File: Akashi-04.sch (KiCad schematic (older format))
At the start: 14 parts, among them CN10 PPPC192LFBN-RC, CN7 PPPC192LFBN-RC

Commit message: Designe done
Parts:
- removed D3, D4: LED, LED_THT:LED_D3.0mm_Clear, symbol Device:LED
- removed R4: 1k, Resistor_THT:R_Axial_DIN0207_L6.3mm_D2.5mm_P10.16mm_Horizontal, symbol Device:R
- removed TP11, TP12: GND, TestPoint:TestPoint_THTPad_D2.0mm_Drill1.0mm, symbol Connector:TestPoint
- added CN5: Conn_01x10, Connector_PinHeader_2.54mm:PinHeader_1x10_P2.54mm_Vertical, symbol Connector_Generic:Conn_01x10
- added CN6, CN9: Conn_01x08, Connector_PinHeader_2.54mm:PinHeader_1x08_P2.54mm_Vertical, symbol Connector_Generic:Conn_01x08
- added CN8: Conn_01x06, Connector_PinHeader_2.54mm:PinHeader_1x06_P2.54mm_Vertical, symbol Connector_Generic:Conn_01x06
- added JP1, JP2: SolderJumper_2_Bridged, Jumper:SolderJumper-2_P1.3mm_Bridged_RoundedPad1.0x1.5mm, symbol Jumper:SolderJumper_2_Bridged
- added JP3, JP4: SolderJumper_2_Open, Jumper:SolderJumper-2_P1.3mm_Open_RoundedPad1.0x1.5mm, symbol Jumper:SolderJumper_2_Open
- added U1: UMB-ADAU1361A, Codec_Modules:UMB-ADAU1361A, symbol Codec_Modules:UMB-ADAU1361A
- R3: value 1k -> 4.7k
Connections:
- net labels removed: LED3, LED4, SW1
- wire segments 51 -> 102
- no-connect marks 56 -> 35
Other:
- note added: "Address\n0x38 – Default\n0x39\n0x3A\n0x3B"
- note added: "Codec I2C Address"
- note added: "JP1\nClosed\nOpen\nClosed\nOpen"
- note added: "JP2\nClosed\nClosed\nOpen\nOpen"
- note added: "JP3\nOpen\nClosed\nOpen\nClosed"
- note added: "JP4\nOpen\nOpen\nClosed\nClosed\n"
- moved on the sheet: R5, R9

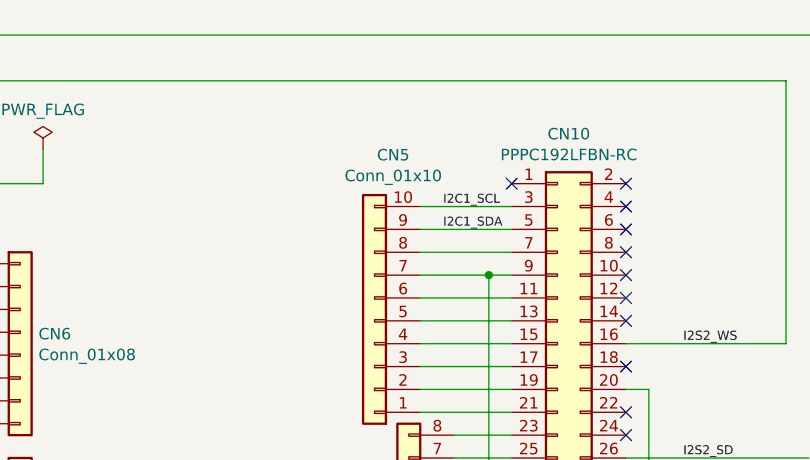
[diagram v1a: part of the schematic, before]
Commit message: Added I2C clock rescue
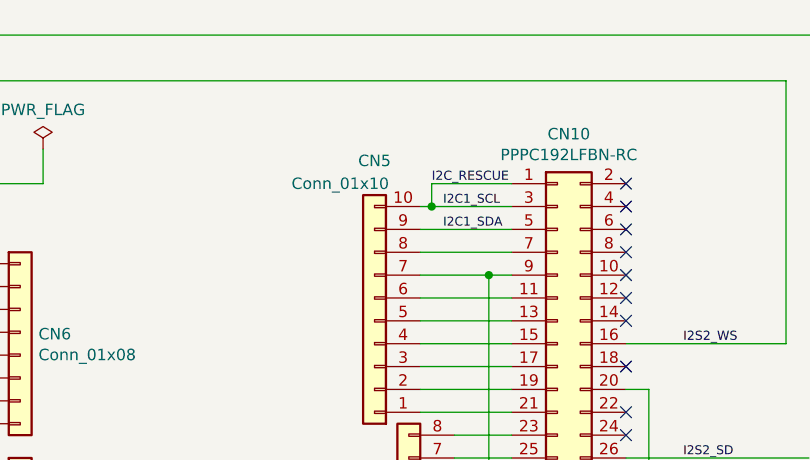
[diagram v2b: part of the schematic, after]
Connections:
- net labels added: I2C_RESCUE
- wire segments 102 -> 105
- no-connect marks 35 -> 34
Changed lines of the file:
@@
 NoConn ~ 5500 2850
 NoConn ~ 5500 2750
-NoConn ~ 8600 2600
 NoConn ~ 9100 2600
 NoConn ~ 9100 2700
@@
 	6550 2450 6550 2600
 Wire Wire Line
-	8200 2700 8600 2700
+	8200 2700 8250 2700
 Wire Wire Line
 	9100 3300 9800 3300
@@
 U 1 1 5E4951B5
 P 8000 3200
-F 0 "CN5" H 7918 2475 50  0000 C CNN
-F 1 "Conn_01x10" H 7918 2566 50  0000 C CNN
+F 0 "CN5" H 8000 2500 50  0000 C CNN
+F 1 "Conn_01x10" H 8150 2600 50  0000 C CNN
 F 2 "Connector_PinHeader_2.54mm:PinHeader_1x10_P2.54mm_Vertical" H 8000 3200 50  0001 C CNN
 F 3 "~" H 8000 3200 50  0001 C CNN
@@
 NoConn ~ 5500 3550
 NoConn ~ 6000 3750
+Wire Wire Line
+	8600 2600 8250 2600
+Wire Wire Line
+	8250 2600 8250 2700
+Connection ~ 8250 2700
+Wire Wire Line
+	8250 2700 8600 2700
+Text Label 8250 2600 0    40   ~ 0
+I2C_RESCUE
 $EndSCHEMATC

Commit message: Added rescue line of I2C and I2S WS int
I2C rescue is needed to toggle the I2C SCL inc case of
the device is stretching signal by fault.

I2S WS int is needed to start the audio in the correct timing.
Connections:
- net labels added: WS_INT
- wire segments 105 -> 107
- no-connect marks 34 -> 33
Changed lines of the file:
@@
 Text Label 3400 3500 0    40   ~ 0
 I2S3_WS
-NoConn ~ 5500 3550
 NoConn ~ 6000 3750
 Wire Wire Line
@@
 Text Label 8250 2600 0    40   ~ 0
 I2C_RESCUE
+Wire Wire Line
+	5500 3550 5000 3550
+Wire Wire Line
+	5000 3550 5000 3350
+Connection ~ 5000 3350
+Text Label 5100 3550 0    40   ~ 0
+WS_INT
 $EndSCHEMATC

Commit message: Generated v1.0.0 gerber
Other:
- note added: "For the default case, R3 can be removed."
- note added: "I2S2 : Slave TX\nI2S3 : Slave RX\nI2C_RESCUE : OD\nWS_INT : EXTI"
- moved on the sheet: R9
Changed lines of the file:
@@
 encoding utf-8
 Sheet 1 1
-Title "AKASHI-01"
-Date "2019-11-04"
-Rev "v1.0.2"
+Title "AKASHI-04"
+Date "2020-03-01"
+Rev "v1.0.0"
 Comp ""
-Comment1 "Test jig for Nucleo 64"
+Comment1 "Audio board for Nucleo G431RB"
 Comment2 ""
 Comment3 ""
@@
 L Device:R R9
 U 1 1 5C988D65
-P 1300 2400
-F 0 "R9" H 1370 2446 50  0000 L CNN
-F 1 "2.2k" H 1370 2355 50  0000 L CNN
-F 2 "Resistor_THT:R_Axial_DIN0207_L6.3mm_D2.5mm_P10.16mm_Horizontal" V 1230 2400 50  0001 C CNN
-F 3 "~" H 1300 2400 50  0001 C CNN
-	1    1300 2400
+P 1250 2400
+F 0 "R9" H 1320 2446 50  0000 L CNN
+F 1 "2.2k" H 1320 2355 50  0000 L CNN
+F 2 "Resistor_THT:R_Axial_DIN0207_L6.3mm_D2.5mm_P10.16mm_Horizontal" V 1180 2400 50  0001 C CNN
+F 3 "~" H 1250 2400 50  0001 C CNN
+	1    1250 2400
 	1    0    0    -1
 $EndComp
@@
 L power:+3.3V #PWR012
 U 1 1 5C98C512
-P 1300 2100
-F 0 "#PWR012" H 1300 1950 50  0001 C CNN
-F 1 "+3.3V" H 1315 2273 50  0000 C CNN
-F 2 "" H 1300 2100 50  0001 C CNN
-F 3 "" H 1300 2100 50  0001 C CNN
-	1    1300 2100
-	1    0    0    -1
-$EndComp
-Wire Wire Line
-	1300 2100 1300 2250
+P 1250 2100
+F 0 "#PWR012" H 1250 1950 50  0001 C CNN
+F 1 "+3.3V" H 1265 2273 50  0000 C CNN
+F 2 "" H 1250 2100 50  0001 C CNN
+F 3 "" H 1250 2100 50  0001 C CNN
+	1    1250 2100
+	1    0    0    -1
+$EndComp
+Wire Wire Line
+	1250 2100 1250 2250
 Wire Wire Line
 	1550 2100 1550 2250
@@
 	1550 2550 1550 3200
 Wire Wire Line
-	1950 3300 1300 3300
-Wire Wire Line
-	1300 2550 1300 3300
+	1950 3300 1250 3300
+Wire Wire Line
+	1250 2550 1250 3300
 $Comp
 L power:+3.3V #PWR06
@@
 Text Label 5100 3550 0    40   ~ 0
 WS_INT
+Text Notes 6600 5000 0    40   ~ 0
+I2S2 : Slave TX\nI2S3 : Slave RX\nI2C_RESCUE : OD\nWS_INT : EXTI
+Text Notes 2100 5100 0    40   ~ 0
+For the default case, R3 can be removed.
 $EndSCHEMATC

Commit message: Update v1.0.1
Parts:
- removed JP3, JP4: SolderJumper_2_Open, Jumper:SolderJumper-2_P1.3mm_Open_RoundedPad1.0x1.5mm, symbol Jumper:SolderJumper_2_Open
- added R4: 4.7k, Resistor_THT:R_Axial_DIN0207_L6.3mm_D2.5mm_P10.16mm_Horizontal, symbol Device:R
- renumbered R9 to R6
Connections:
- wire segments 107 -> 106
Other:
- note added: "R3 and R4 must be installed only when JP1 and JP2 is cut, respectively"
- note removed: "For the default case, R3 can be removed."
- note removed: "JP3\nOpen\nClosed\nOpen\nClosed"
- note removed: "JP4\nOpen\nOpen\nClosed\nClosed\n"
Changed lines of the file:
@@
 	8200 2800 8600 2800
-$Comp
-L Device:R R9
-U 1 1 5C988D65
-P 1250 2400
-F 0 "R9" H 1320 2446 50  0000 L CNN
-F 1 "2.2k" H 1320 2355 50  0000 L CNN
-F 2 "Resistor_THT:R_Axial_DIN0207_L6.3mm_D2.5mm_P10.16mm_Horizontal" V 1180 2400 50  0001 C CNN
-F 3 "~" H 1250 2400 50  0001 C CNN
-	1    1250 2400
-	1    0    0    -1
-$EndComp
-$Comp
-L Device:R R5
-U 1 1 5C989336
-P 1550 2400
-F 0 "R5" H 1620 2446 50  0000 L CNN
-F 1 "2.2k" H 1620 2355 50  0000 L CNN
-F 2 "Resistor_THT:R_Axial_DIN0207_L6.3mm_D2.5mm_P10.16mm_Horizontal" V 1480 2400 50  0001 C CNN
-F 3 "~" H 1550 2400 50  0001 C CNN
-	1    1550 2400
-	1    0    0    -1
-$EndComp
 $Comp
 L power:+3.3V #PWR09
@@
 	0    1    1    0
 $EndComp
-$Comp
-L Jumper:SolderJumper_2_Open JP3
-U 1 1 5E5272BE
-P 3650 3700
-F 0 "JP3" H 3650 3813 50  0000 C CNN
-F 1 "SolderJumper_2_Open" H 3650 3814 50  0001 C CNN
-F 2 "Jumper:SolderJumper-2_P1.3mm_Open_RoundedPad1.0x1.5mm" H 3650 3700 50  0001 C CNN
-F 3 "~" H 3650 3700 50  0001 C CNN
-	1    3650 3700
-	1    0    0    -1
-$EndComp
-$Comp
-L Jumper:SolderJumper_2_Open JP4
-U 1 1 5E527B62
-P 3650 3800
-F 0 "JP4" H 3650 3700 50  0000 C CNN
-F 1 "SolderJumper_2_Open" H 3650 3914 50  0001 C CNN
-F 2 "Jumper:SolderJumper-2_P1.3mm_Open_RoundedPad1.0x1.5mm" H 3650 3800 50  0001 C CNN
-F 3 "~" H 3650 3800 50  0001 C CNN
-	1    3650 3800
-	1    0    0    -1
-$EndComp
 Wire Wire Line
 	3100 3700 3200 3700
@@
 Connection ~ 3400 3800
 Wire Wire Line
-	3400 3800 3500 3800
-Wire Wire Line
 	3200 3850 3200 3700
 Connection ~ 3200 3700
-Wire Wire Line
-	3200 3700 3500 3700
 NoConn ~ 3100 3000
 NoConn ~ 3100 3100
@@
 	4000 3550 4000 3700
 Wire Wire Line
-	4000 3800 3800 3800
-Wire Wire Line
-	3800 3700 4000 3700
-Connection ~ 4000 3700
-Wire Wire Line
-	4000 3700 4000 3800
-Wire Wire Line
 	4850 5450 4850 5600
 Text Notes 2100 4950 0    40   ~ 0
@@
 Text Notes 2350 4950 0    40   ~ 0
 JP2\nClosed\nClosed\nOpen\nOpen
-Text Notes 2600 4950 0    40   ~ 0
-JP3\nOpen\nClosed\nOpen\nClosed
-Text Notes 2850 4950 0    40   ~ 0
-JP4\nOpen\nOpen\nClosed\nClosed\n
-Text Notes 3100 4950 0    40   ~ 0
+Text Notes 2650 4950 0    40   ~ 0
 Address\n0x38 – Default\n0x39\n0x3A\n0x3B
-Text Notes 2400 4550 0    40   ~ 0
+Text Notes 2250 4550 0    40   ~ 0
 Codec I2C Address
 Wire Wire Line
@@
 I2S2 : Slave TX\nI2S3 : Slave RX\nI2C_RESCUE : OD\nWS_INT : EXTI
 Text Notes 2100 5100 0    40   ~ 0
-For the default case, R3 can be removed.
+R3 and R4 must be installed only when JP1 and JP2 is cut, respectively
+Text Label 1600 3200 0    50   ~ 0
+I2C1_SDA
+Text Label 1600 3300 0    50   ~ 0
+I2C1_SCL
+$Comp
+L Device:R R6
+U 1 1 5C988D65
+P 1250 2400
+F 0 "R6" H 1320 2446 50  0000 L CNN
+F 1 "2.2k" H 1320 2355 50  0000 L CNN
+F 2 "Resistor_THT:R_Axial_DIN0207_L6.3mm_D2.5mm_P10.16mm_Horizontal" V 1180 2400 50  0001 C CNN
+F 3 "~" H 1250 2400 50  0001 C CNN
+	1    1250 2400
+	1    0    0    -1
+$EndComp
+$Comp
+L Device:R R5
+U 1 1 5C989336
+P 1550 2400
+F 0 "R5" H 1620 2446 50  0000 L CNN
+F 1 "2.2k" H 1620 2355 50  0000 L CNN
+F 2 "Resistor_THT:R_Axial_DIN0207_L6.3mm_D2.5mm_P10.16mm_Horizontal" V 1480 2400 50  0001 C CNN
+F 3 "~" H 1550 2400 50  0001 C CNN
+	1    1550 2400
+	1    0    0    -1
+$EndComp
+$Comp
+L Device:R R4
+U 1 1 5E69CA7E
+P 4300 3400
+F 0 "R4" H 4370 3446 50  0000 L CNN
+F 1 "4.7k" H 4370 3355 50  0000 L CNN
+F 2 "Resistor_THT:R_Axial_DIN0207_L6.3mm_D2.5mm_P10.16mm_Horizontal" V 4230 3400 50  0001 C CNN
+F 3 "~" H 4300 3400 50  0001 C CNN
+	1    4300 3400
+	1    0    0    -1
+$EndComp
+$Comp
+L power:+3.3V #PWR0101
+U 1 1 5E69CA88
+P 4300 3100
+F 0 "#PWR0101" H 4300 2950 50  0001 C CNN
+F 1 "+3.3V" H 4315 3273 50  0000 C CNN
+F 2 "" H 4300 3100 50  0001 C CNN
+F 3 "" H 4300 3100 50  0001 C CNN
+	1    4300 3100
+	1    0    0    -1
+$EndComp
+Wire Wire Line
+	4300 3100 4300 3250
+Wire Wire Line
+	4300 3550 4300 3800
+Wire Wire Line
+	3200 3700 4000 3700
+Wire Wire Line
+	3400 3800 4300 3800
 $EndSCHEMATC
